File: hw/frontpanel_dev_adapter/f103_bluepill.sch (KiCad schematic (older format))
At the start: 46 parts, among them J501 Conn_01x20, J502 Conn_01x20, J503 SWD, J504 STX-3501-3N_(TTL-232R-xV-AJ), J505 Conn_01x03, Q501 AO3401A, SW501 SKHUxxE010, U501 STM32F103CBTx, U502 W25Q128JVSIQ, U503 AT24C256C-SSHL, U504 DS3231M, Y501 16MHz

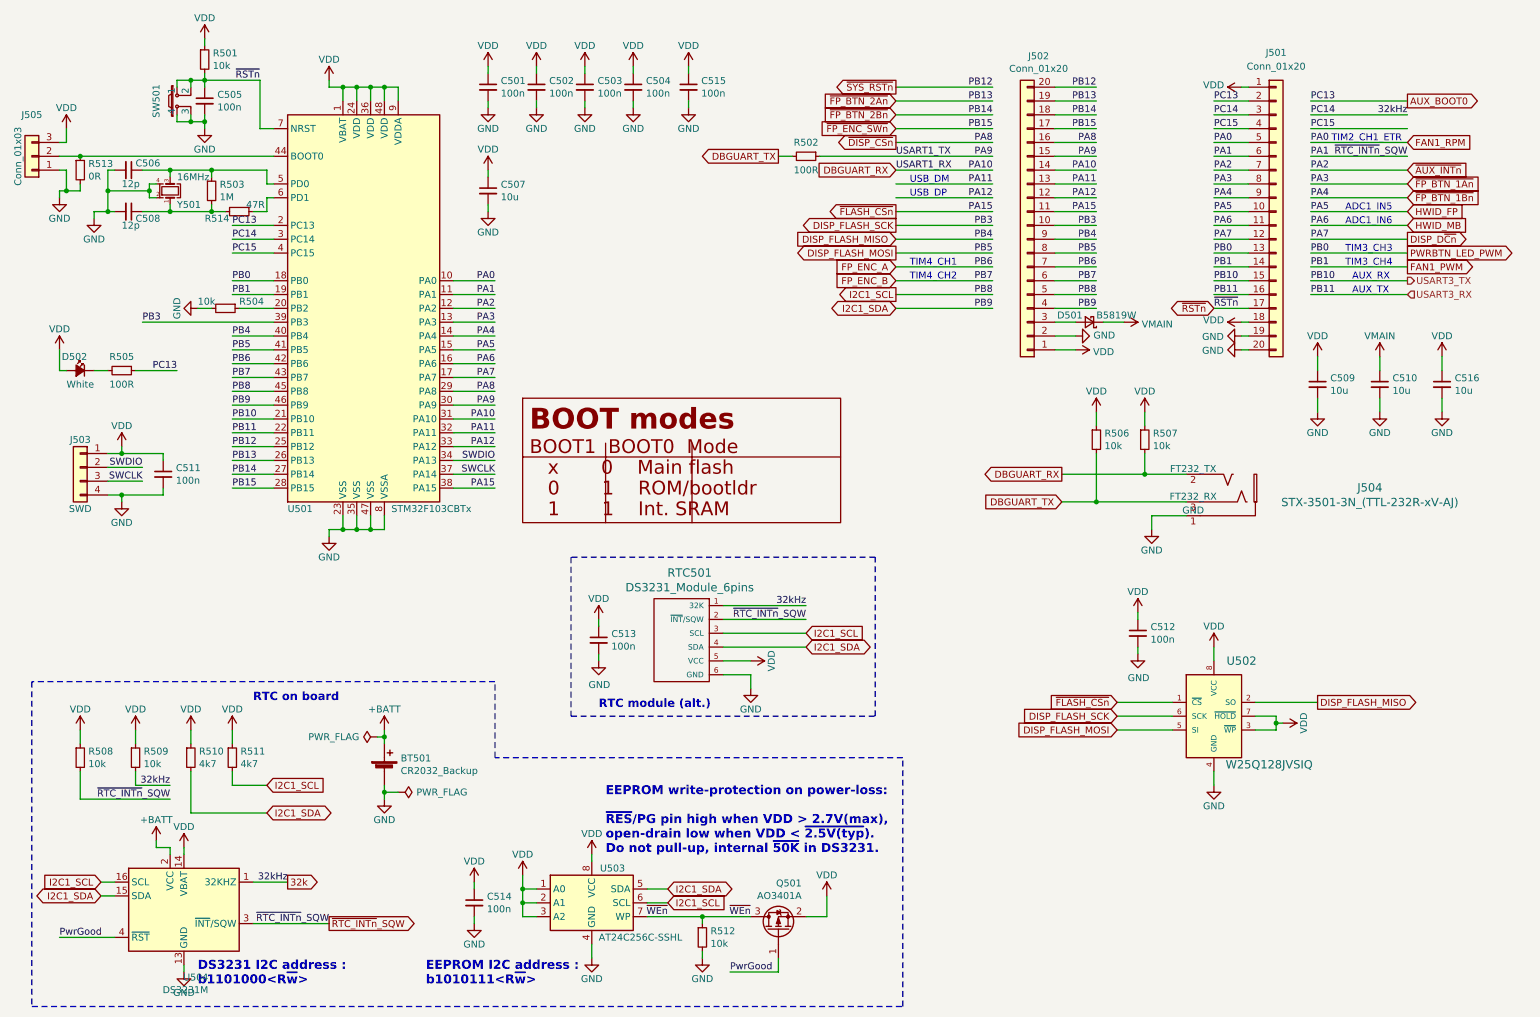
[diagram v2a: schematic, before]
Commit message: FP adapter/dev board: *routing DONE* ; minor pinout tweaks (optimize routing); fix some missing 3d models
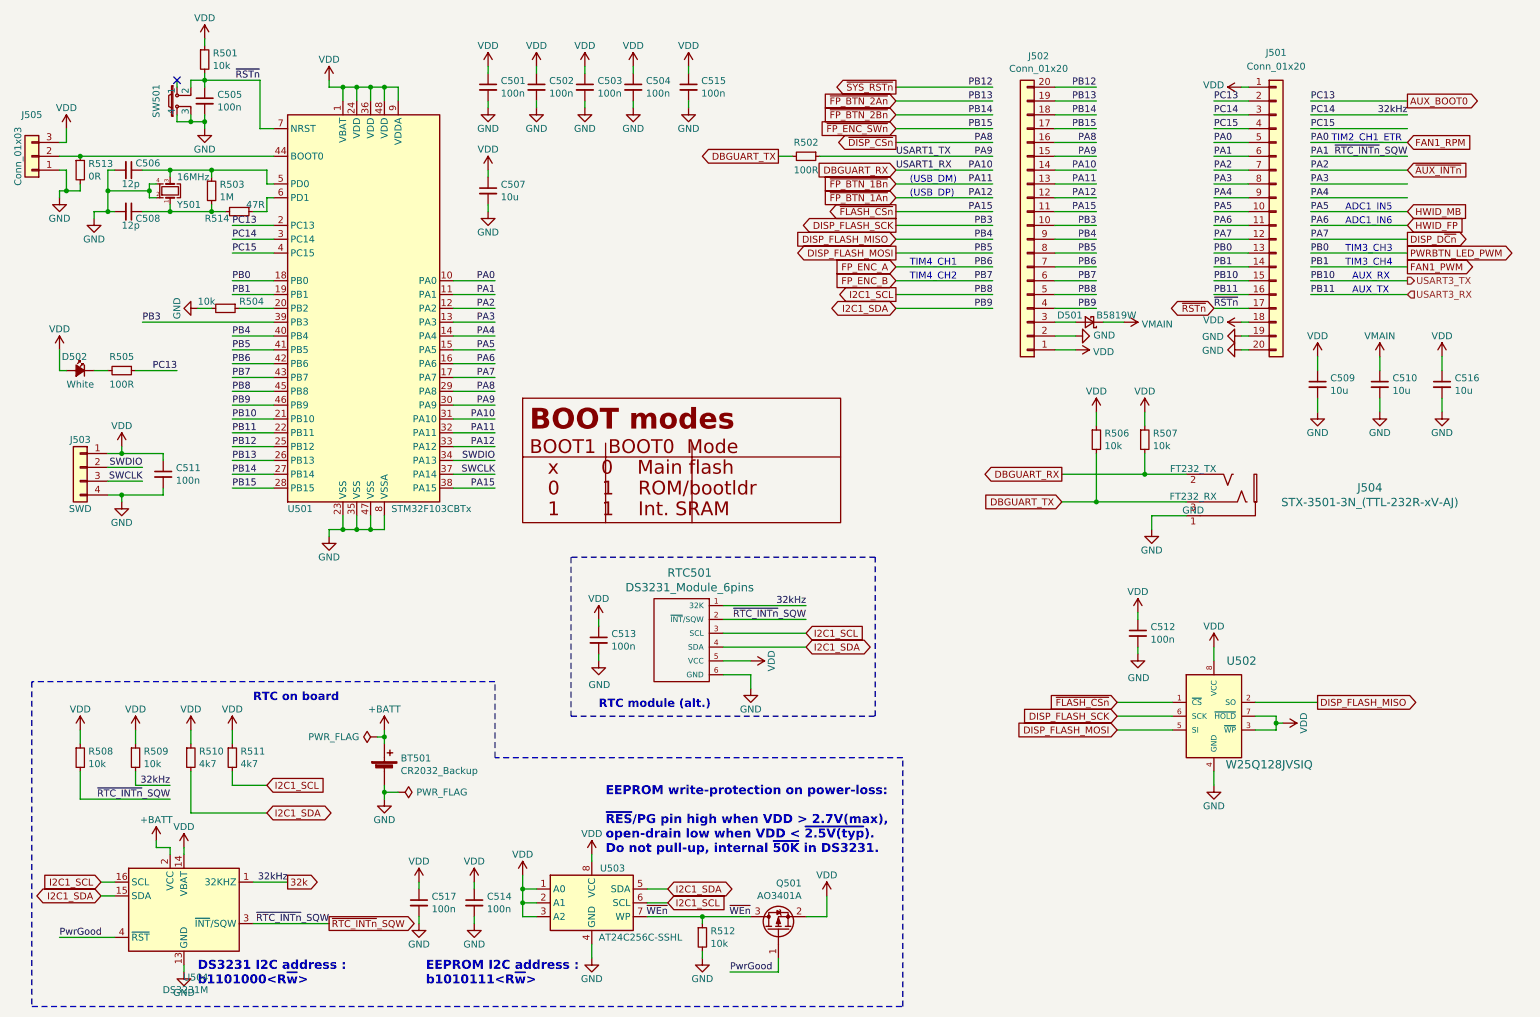
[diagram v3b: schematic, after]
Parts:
- added C517: 100n, Capacitor_SMD:C_0402_1005Metric, symbol Device:C_Small
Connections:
- net PA11 is gone; now on net ~FP_BTN_1Bn~: J502.13 (Pin_13), U501.32 (PA11)
- net PA12 is gone; now on net ~FP_BTN_1An~: J502.12 (Pin_12), U501.33 (PA12)
- net GND: now also C517.2
- net HWID_FP: now also J501.11 (Pin_11), U501.16 (PA6); no longer J501.10 (Pin_10), U501.15 (PA5)
- net HWID_MB: now also J501.10 (Pin_10), U501.15 (PA5); no longer J501.11 (Pin_11), U501.16 (PA6)
- net VDD: now also C517.1
- net ~FP_BTN_1An~: no longer J501.8 (Pin_8), U501.13 (PA3)
- net ~FP_BTN_1Bn~: no longer J501.9 (Pin_9), U501.14 (PA4)
- net ~RSTn~: no longer SW501.1
- new net PA3: J501.8 (Pin_8), U501.13 (PA3)
- new net PA4: J501.9 (Pin_9), U501.14 (PA4)
- no-connect marks 0 -> 1
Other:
- note added: "(USB_DM)"
- note added: "(USB_DP)"
- note removed: "USB_DM"
- note removed: "USB_DP"
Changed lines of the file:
@@
 Text GLabel 10550 2200 2    50   Output ~ 0
 DISP_D~Cn~
-Text GLabel 10550 1800 2    50   Input ~ 0
+Text GLabel 6850 1900 0    50   Input ~ 0
 ~FP_BTN_1An~
-Text GLabel 10550 1900 2    50   Input ~ 0
+Text GLabel 6850 1800 0    50   Input ~ 0
 ~FP_BTN_1Bn~
 Text GLabel 6850 1200 0    50   Input ~ 0
@@
 Text Notes 10100 2300 0    50   ~ 0
 TIM3_CH3
+Text GLabel 10550 2100 2    50   Input ~ 0
+HWID_FP
 Text GLabel 10550 2000 2    50   Input ~ 0
-HWID_FP
-Text GLabel 10550 2100 2    50   Input ~ 0
 HWID_MB
 Text Notes 10100 2000 0    50   ~ 0
@@
 Wire Wire Line
 	1750 1050 1850 1050
-Wire Wire Line
-	1750 1050 1650 1050
-Wire Wire Line
-	1650 1050 1650 1100
-Connection ~ 1750 1050
 Wire Wire Line
 	1650 1300 1650 1350
@@
 	5450 7150 5450 7100
 Text Notes 6950 1800 0    50   ~ 0
-USB_DM
-Text Notes 6950 1900 0    50   ~ 0
-USB_DP
+(USB_DM)
 Wire Wire Line
 	5800 7100 5450 7100
@@
 	1    0    0    -1
 $EndComp
+$Comp
+L Device:C_Small C517
+U 1 1 60495DC1
+P 3400 7000
+F 0 "C517" H 3492 7046 50  0000 L CNN
+F 1 "100n" H 3492 6955 50  0000 L CNN
+F 2 "Capacitor_SMD:C_0402_1005Metric" H 3400 7000 50  0001 C CNN
+F 3 "~" H 3400 7000 50  0001 C CNN
+	1    3400 7000
+	1    0    0    -1
+$EndComp
+$Comp
+L power:GND #PWR0566
+U 1 1 60496669
+P 3400 7150
+F 0 "#PWR0566" H 3400 6900 50  0001 C CNN
+F 1 "GND" H 3400 7000 50  0000 C CNN
+F 2 "" H 3400 7150 50  0001 C CNN
+F 3 "" H 3400 7150 50  0001 C CNN
+	1    3400 7150
+	1    0    0    -1
+$EndComp
+Wire Wire Line
+	3400 7150 3400 7100
+$Comp
+L power:VDD #PWR0565
+U 1 1 60496674
+P 3400 6850
+F 0 "#PWR0565" H 3400 6700 50  0001 C CNN
+F 1 "VDD" H 3400 7000 50  0000 C CNN
+F 2 "" H 3400 6850 50  0001 C CNN
+F 3 "" H 3400 6850 50  0001 C CNN
+	1    3400 6850
+	1    0    0    -1
+$EndComp
+Wire Wire Line
+	3400 6850 3400 6900
+NoConn ~ 1650 1050
+Wire Wire Line
+	1650 1100 1650 1050
+Text Notes 6950 1900 0    50   ~ 0
+(USB_DP)
 $EndSCHEMATC

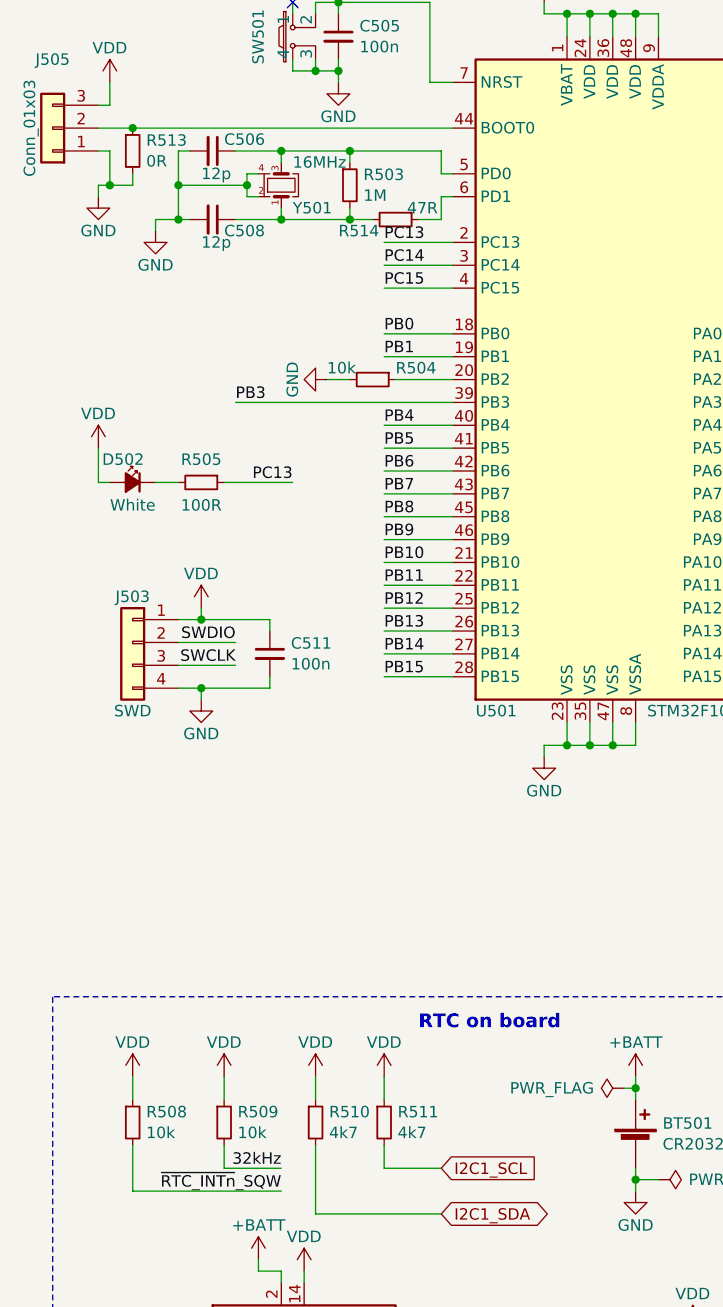
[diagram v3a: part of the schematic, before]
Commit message: FP adapter board: Added LCSC partnumbers to all components to be PnP:ed; Finalized some silk additions; Generated Gerbers, BoM & pnp-files for JCL assembly
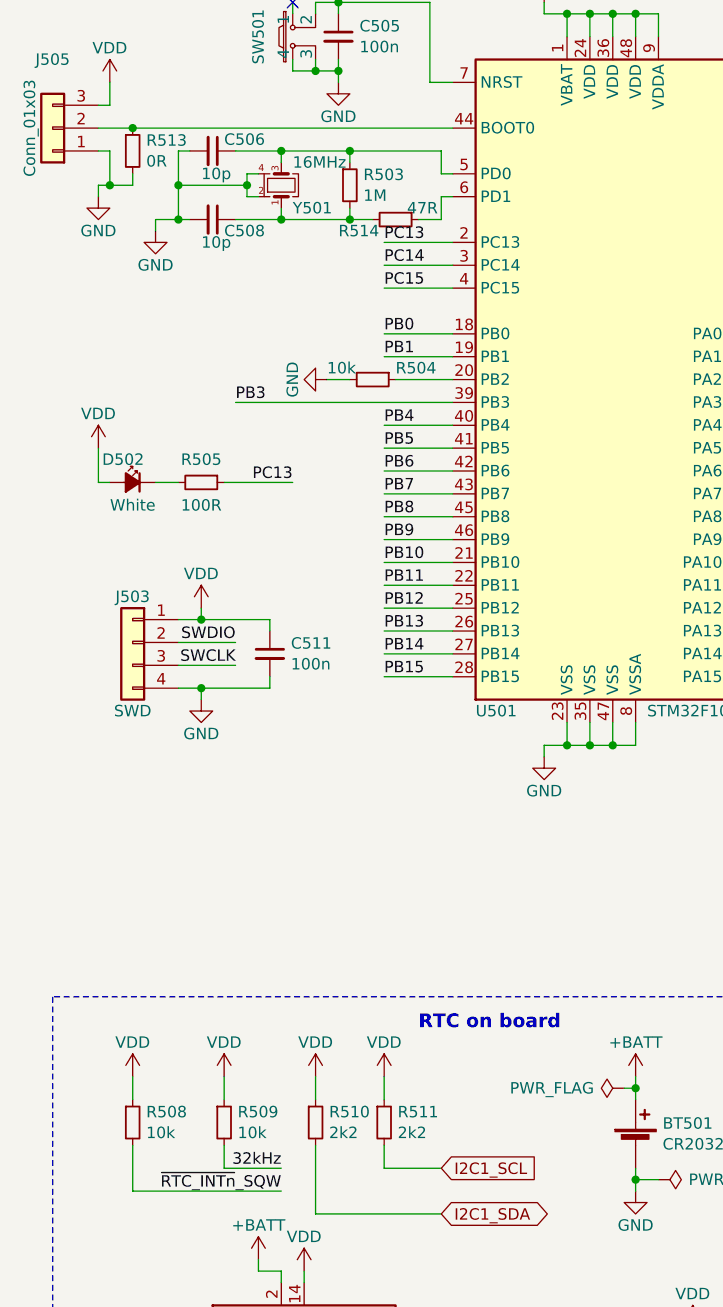
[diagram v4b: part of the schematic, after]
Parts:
- C501, C502, C503, C504, C505, C511, C512, C513, C514, C515, C517: LCSC (none) -> C1525
- C506, C508: value 12p -> 10p; LCSC (none) -> C32949
- C507, C509, C510, C516: LCSC (none) -> C19702
- D501: LCSC (none) -> C8598
- D502: LCSC (none) -> C2290
- Q501: LCSC (none) -> C15127
- R501, R504, R506, R508, R509, R512: LCSC (none) -> C25744
- R502, R505: LCSC (none) -> C25076
- R503: LCSC (none) -> C26083
- R507: Field4 (none) -> C25744
- R510, R511: value 4k7 -> 2k2; LCSC (none) -> C25879
- R513: LCSC (none) -> C17168
- R514: LCSC (none) -> C25118
- U501: LCSC (none) -> C8304
- U502: LCSC (none) -> C97521
- U503: LCSC (none) -> C6482
- U504: LCSC (none) -> C37663
- Y501: LCSC (none) -> C13738
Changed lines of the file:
@@
 F 2 "Capacitor_SMD:C_0603_1608Metric" H 9900 3250 50  0001 C CNN
 F 3 "~" H 9900 3250 50  0001 C CNN
+F 4 "C19702" H 9900 3250 50  0001 C CNN "LCSC"
 	1    9900 3250
 	1    0    0    -1
@@
 F 2 "Resistor_SMD:R_0402_1005Metric" H 8300 3650 50  0001 C CNN
 F 3 "~" H 8300 3650 50  0001 C CNN
+F 4 "C25744" H 8300 3650 50  0001 C CNN "LCSC"
 	1    8300 3650
 	1    0    0    -1
@@
 F 2 "Resistor_SMD:R_0402_1005Metric" H 8650 3650 50  0001 C CNN
 F 3 "~" H 8650 3650 50  0001 C CNN
+F 4 "C25744" H 8650 3650 50  0001 C CNN "Field4"
 	1    8650 3650
 	1    0    0    -1
@@
 F 2 "Package_SO:SOIC-8_5.23x5.23mm_P1.27mm" H 9150 5650 60  0001 C CNN
 F 3 "https://www.pjrc.com/store/w25q64fv.pdf" H 9150 5650 60  0001 C CNN
+F 4 "C97521" H 9150 5650 50  0001 C CNN "LCSC"
 	1    9150 5650
 	1    0    0    -1
@@
 F 2 "Capacitor_SMD:C_0402_1005Metric" H 8600 5050 50  0001 C CNN
 F 3 "~" H 8600 5050 50  0001 C CNN
+F 4 "C1525" H 8600 5050 50  0001 C CNN "LCSC"
 	1    8600 5050
 	1    0    0    -1
@@
 F 2 "Capacitor_SMD:C_0402_1005Metric" H 4700 5100 50  0001 C CNN
 F 3 "~" H 4700 5100 50  0001 C CNN
+F 4 "C1525" H 4700 5100 50  0001 C CNN "LCSC"
 	1    4700 5100
 	1    0    0    -1
@@
 F 2 "Package_QFP:LQFP-48_7x7mm_P0.5mm" H 2450 1300 50  0001 R CNN
 F 3 "http://www.st.com/st-web-ui/static/active/en/resource/technical/document/datasheet/CD00161566.pdf" H 3050 2700 50  0001 C CNN
+F 4 "C8304" H 3050 2700 50  0001 C CNN "LCSC"
 	1    3050 2700
 	1    0    0    -1
@@
 F 2 "Capacitor_SMD:C_0402_1005Metric" H 3900 1100 50  0001 C CNN
 F 3 "~" H 3900 1100 50  0001 C CNN
+F 4 "C1525" H 3900 1100 50  0001 C CNN "LCSC"
 	1    3900 1100
 	1    0    0    -1
@@
 F 2 "Capacitor_SMD:C_0402_1005Metric" H 4250 1100 50  0001 C CNN
 F 3 "~" H 4250 1100 50  0001 C CNN
+F 4 "C1525" H 4250 1100 50  0001 C CNN "LCSC"
 	1    4250 1100
 	1    0    0    -1
@@
 F 2 "Capacitor_SMD:C_0402_1005Metric" H 4600 1100 50  0001 C CNN
 F 3 "~" H 4600 1100 50  0001 C CNN
+F 4 "C1525" H 4600 1100 50  0001 C CNN "LCSC"
 	1    4600 1100
 	1    0    0    -1
@@
 F 2 "Capacitor_SMD:C_0402_1005Metric" H 4950 1100 50  0001 C CNN
 F 3 "~" H 4950 1100 50  0001 C CNN
+F 4 "C1525" H 4950 1100 50  0001 C CNN "LCSC"
 	1    4950 1100
 	1    0    0    -1
@@
 F 2 "Capacitor_SMD:C_0603_1608Metric" H 3900 1850 50  0001 C CNN
 F 3 "~" H 3900 1850 50  0001 C CNN
+F 4 "C19702" H 3900 1850 50  0001 C CNN "LCSC"
 	1    3900 1850
 	1    0    0    -1
@@
 F 2 "Capacitor_SMD:C_0603_1608Metric" H 10350 3250 50  0001 C CNN
 F 3 "~" H 10350 3250 50  0001 C CNN
+F 4 "C19702" H 10350 3250 50  0001 C CNN "LCSC"
 	1    10350 3250
 	1    0    0    -1
@@
 F 2 "Resistor_SMD:R_0402_1005Metric" H 1850 900 50  0001 C CNN
 F 3 "~" H 1850 900 50  0001 C CNN
+F 4 "C25744" H 1850 900 50  0001 C CNN "LCSC"
 	1    1850 900
 	1    0    0    -1
@@
 F 2 "Capacitor_SMD:C_0402_1005Metric" H 1850 1200 50  0001 C CNN
 F 3 "~" H 1850 1200 50  0001 C CNN
+F 4 "C1525" H 1850 1200 50  0001 C CNN "LCSC"
 	1    1850 1200
 	1    0    0    -1
@@
 F 2 "Resistor_SMD:R_0402_1005Metric" H 2000 2700 50  0001 C CNN
 F 3 "~" H 2000 2700 50  0001 C CNN
+F 4 "C25744" V 2000 2700 50  0001 C CNN "LCSC"
 	1    2000 2700
 	0    1    1    0
@@
 F 2 "Crystal:Crystal_SMD_3225-4Pin_3.2x2.5mm" H 1600 1850 50  0001 C CNN
 F 3 "https://datasheet.lcsc.com/szlcsc/Yangxing-Tech-X322516MLB4SI_C13738.pdf" H 1600 1850 50  0001 C CNN
+F 4 "C13738" V 1600 1850 50  0001 C CNN "LCSC"
 	1    1600 1850
 	0    1    -1   0
@@
 F 2 "Resistor_SMD:R_0402_1005Metric" H 1900 1850 50  0001 C CNN
 F 3 "~" H 1900 1850 50  0001 C CNN
+F 4 "C26083" H 1900 1850 50  0001 C CNN "LCSC"
 	1    1900 1850
 	1    0    0    -1
@@
 P 1300 1700
 F 0 "C506" V 1250 1750 50  0000 L CNN
-F 1 "12p" V 1400 1650 50  0000 L CNN
+F 1 "10p" V 1400 1650 50  0000 L CNN
 F 2 "Capacitor_SMD:C_0402_1005Metric" H 1300 1700 50  0001 C CNN
 F 3 "~" H 1300 1700 50  0001 C CNN
+F 4 "C32949" V 1300 1700 50  0001 C CNN "LCSC"
 	1    1300 1700
 	0    1    1    0
@@
 P 1300 2000
 F 0 "C508" V 1350 2050 50  0000 L CNN
-F 1 "12p" V 1400 1950 50  0000 L CNN
+F 1 "10p" V 1400 1950 50  0000 L CNN
 F 2 "Capacitor_SMD:C_0402_1005Metric" H 1300 2000 50  0001 C CNN
 F 3 "~" H 1300 2000 50  0001 C CNN
+F 4 "C32949" V 1300 2000 50  0001 C CNN "LCSC"
 	1    1300 2000
 	0    1    1    0
@@
 F 2 "Resistor_SMD:R_0402_1005Metric" H 1250 3150 50  0001 C CNN
 F 3 "~" H 1250 3150 50  0001 C CNN
+F 4 "C25076" V 1250 3150 50  0001 C CNN "LCSC"
 	1    1250 3150
 	0    1    1    0
@@
 F 2 "LED_SMD:LED_0603_1608Metric" V 950 3150 50  0001 C CNN
 F 3 "~" V 950 3150 50  0001 C CNN
+F 4 "C2290" H 950 3150 50  0001 C CNN "LCSC"
 	1    950  3150
 	-1   0    0    -1
@@
 F 2 "Capacitor_SMD:C_0402_1005Metric" H 1550 3900 50  0001 C CNN
 F 3 "~" H 1550 3900 50  0001 C CNN
+F 4 "C1525" H 1550 3900 50  0001 C CNN "LCSC"
 	1    1550 3900
 	1    0    0    -1
@@
 F 2 "Resistor_SMD:R_0402_1005Metric" H 950 5950 50  0001 C CNN
 F 3 "~" H 950 5950 50  0001 C CNN
+F 4 "C25744" H 950 5950 50  0001 C CNN "LCSC"
 	1    950  5950
 	1    0    0    -1
@@
 F 2 "Resistor_SMD:R_0402_1005Metric" H 1350 5950 50  0001 C CNN
 F 3 "~" H 1350 5950 50  0001 C CNN
+F 4 "C25744" H 1350 5950 50  0001 C CNN "LCSC"
 	1    1350 5950
 	1    0    0    -1
@@
 P 1750 5950
 F 0 "R510" H 1809 5996 50  0000 L CNN
-F 1 "4k7" H 1809 5905 50  0000 L CNN
+F 1 "2k2" H 1809 5905 50  0000 L CNN
 F 2 "Resistor_SMD:R_0402_1005Metric" H 1750 5950 50  0001 C CNN
 F 3 "~" H 1750 5950 50  0001 C CNN
+F 4 "C25879" H 1750 5950 50  0001 C CNN "LCSC"
 	1    1750 5950
 	1    0    0    -1
@@
 P 2050 5950
 F 0 "R511" H 2109 5996 50  0000 L CNN
-F 1 "4k7" H 2109 5905 50  0000 L CNN
+F 1 "2k2" H 2109 5905 50  0000 L CNN
 F 2 "Resistor_SMD:R_0402_1005Metric" H 2050 5950 50  0001 C CNN
 F 3 "~" H 2050 5950 50  0001 C CNN
+F 4 "C25879" H 2050 5950 50  0001 C CNN "LCSC"
 	1    2050 5950
 	1    0    0    -1
@@
 F 2 "Capacitor_SMD:C_0402_1005Metric" H 3800 7000 50  0001 C CNN
 F 3 "~" H 3800 7000 50  0001 C CNN
+F 4 "C1525" H 3800 7000 50  0001 C CNN "LCSC"
 	1    3800 7000
 	1    0    0    -1
@@
 F 2 "Package_SO:SO-8_3.9x4.9mm_P1.27mm" H 4650 7000 50  0001 C CNN
 F 3 "https://datasheet.lcsc.com/szlcsc/Microchip-Tech-AT24C256C-SSHL-T_C6482.pdf" H 4650 7000 50  0001 C CNN
+F 4 "C6482" H 4650 7000 50  0001 C CNN "LCSC"
 	1    4650 7000
 	1    0    0    -1
@@
 F 2 "Package_TO_SOT_SMD:SOT-23" H 6200 7125 50  0001 L CIN
 F 3 "http://www.aosmd.com/pdfs/datasheet/AO3401A.pdf" H 6000 7200 50  0001 L CNN
+F 4 "C15127" V 6000 7200 50  0001 C CNN "LCSC"
 	1    6000 7200
 	0    -1   -1   0
@@
 F 2 "Resistor_SMD:R_0402_1005Metric" H 6200 1600 50  0001 C CNN
 F 3 "~" H 6200 1600 50  0001 C CNN
+F 4 "C25076" V 6200 1600 50  0001 C CNN "LCSC"
 	1    6200 1600
 	0    1    1    0
@@
 F 2 "Resistor_SMD:R_0402_1005Metric" H 5450 7250 50  0001 C CNN
 F 3 "~" H 5450 7250 50  0001 C CNN
+F 4 "C25744" H 5450 7250 50  0001 C CNN "LCSC"
 	1    5450 7250
 	1    0    0    -1
@@
 F 2 "Capacitor_SMD:C_0402_1005Metric" H 5350 1100 50  0001 C CNN
 F 3 "~" H 5350 1100 50  0001 C CNN
+F 4 "C1525" H 5350 1100 50  0001 C CNN "LCSC"
 	1    5350 1100
 	1    0    0    -1
@@
 F 2 "Diode_SMD:D_SOD-123" V 8250 2800 50  0001 C CNN
 F 3 "https://datasheet.lcsc.com/szlcsc/Changjiang-Electronics-Tech-CJ-B5819W_C8598.pdf" V 8250 2800 50  0001 C CNN
+F 4 "C8598" H 8250 2800 50  0001 C CNN "LCSC"
 	1    8250 2800
 	-1   0    0    1
@@
 F 2 "Resistor_SMD:R_0402_1005Metric" H 950 1700 50  0001 C CNN
 F 3 "~" H 950 1700 50  0001 C CNN
+F 4 "C17168" H 950 1700 50  0001 C CNN "LCSC"
 	1    950  1700
 	1    0    0    -1
@@
 F 2 "Resistor_SMD:R_0402_1005Metric" H 2100 2000 50  0001 C CNN
 F 3 "~" H 2100 2000 50  0001 C CNN
+F 4 "C25118" V 2100 2000 50  0001 C CNN "LCSC"
 	1    2100 2000
 	0    1    1    0
@@
 F 2 "Capacitor_SMD:C_0603_1608Metric" H 10800 3250 50  0001 C CNN
 F 3 "~" H 10800 3250 50  0001 C CNN
+F 4 "C19702" H 10800 3250 50  0001 C CNN "LCSC"
 	1    10800 3250
 	1    0    0    -1
@@
 F 2 "Package_SO:SOIC-16W_7.5x10.3mm_P1.27mm" H 1700 6450 50  0001 C CNN
 F 3 "http://datasheets.maximintegrated.com/en/ds/DS3231.pdf" H 1970 7100 50  0001 C CNN
+F 4 "C37663" H 1700 7050 50  0001 C CNN "LCSC"
 	1    1700 7050
 	1    0    0    -1
@@
 F 2 "Capacitor_SMD:C_0402_1005Metric" H 3400 7000 50  0001 C CNN
 F 3 "~" H 3400 7000 50  0001 C CNN
+F 4 "C1525" H 3400 7000 50  0001 C CNN "LCSC"
 	1    3400 7000
 	1    0    0    -1
